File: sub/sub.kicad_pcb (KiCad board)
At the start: 2 copper layers, 54 x 160 mm, 17 parts, among them J1 YG_IN, J2 YG_OUT, J3 PBB_IN, J4 PBB_OUT, J5 PRR_IN, J6 PRR_OUT, J7 SYNC_IN, J8 SYNC_OUT, J9 Conn_01x05, SW1 SW_YG_TERM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

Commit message: Add main PCB
Also some minor tweaks.
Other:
- outline, holes or cut-outs redrawn
- board text added: "R1-4 - 75R All 0805 size / 1% SW1-4 - JS202011SCQN J9 - JST NH BS5P-SHF-1AA"
- board text removed: "R1-4 - 75Ω All 0805 size / 1% SW1-4 - JS202011SCQN"

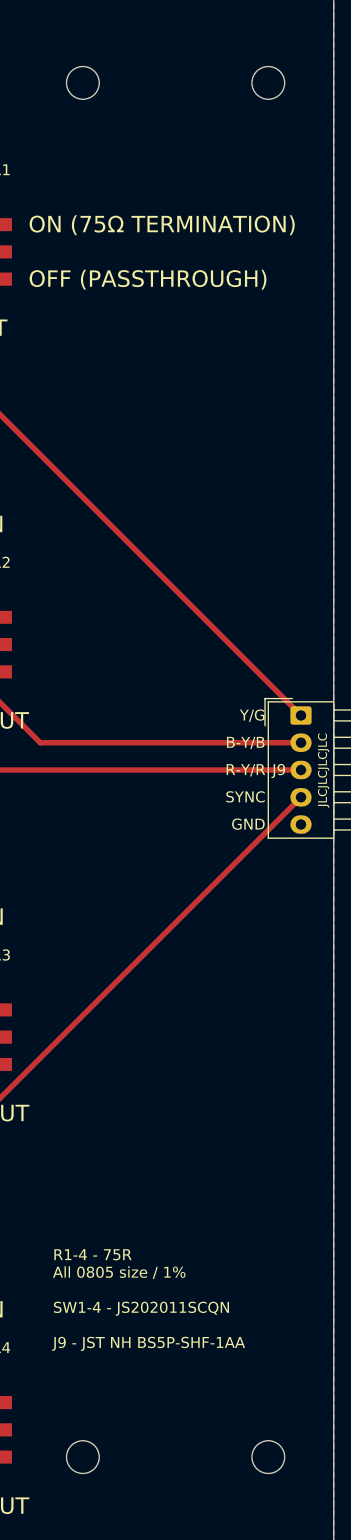
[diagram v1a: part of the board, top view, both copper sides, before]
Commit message: Use proper mounting holes rather than edge cuts
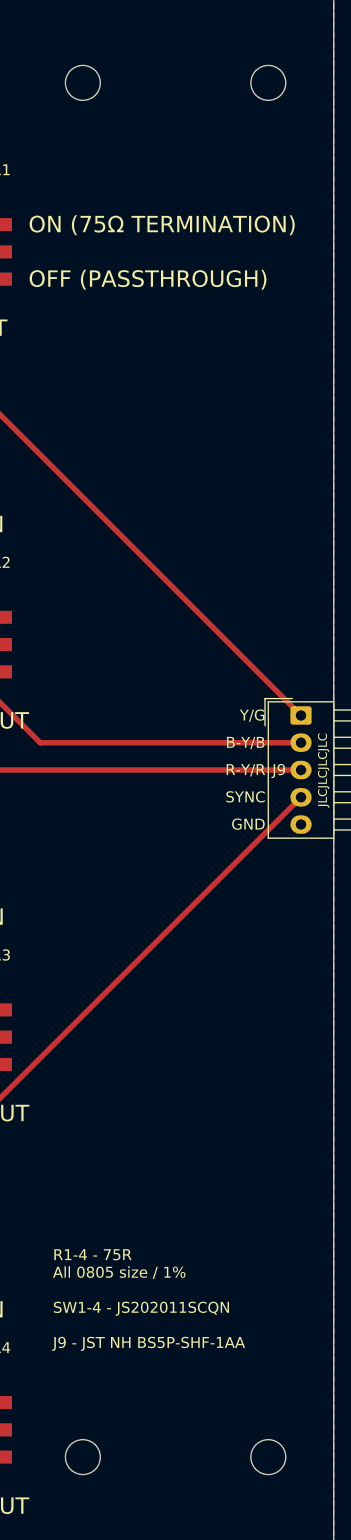
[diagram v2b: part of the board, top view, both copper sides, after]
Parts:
- added H1: MountingHole, MountingHole:MountingHole_3.2mm_M3, F.Cu at (71.0, 37.0)
- added H2: MountingHole, MountingHole:MountingHole_3.2mm_M3, F.Cu at (88.0, 37.0)
- added H3: MountingHole, MountingHole:MountingHole_3.2mm_M3, F.Cu at (71.0, 163.0)
- added H4: MountingHole, MountingHole:MountingHole_3.2mm_M3, F.Cu at (88.0, 163.0)
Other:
- outline, holes or cut-outs redrawn
